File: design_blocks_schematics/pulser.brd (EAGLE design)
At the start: 160 x 100 mm, 52 parts

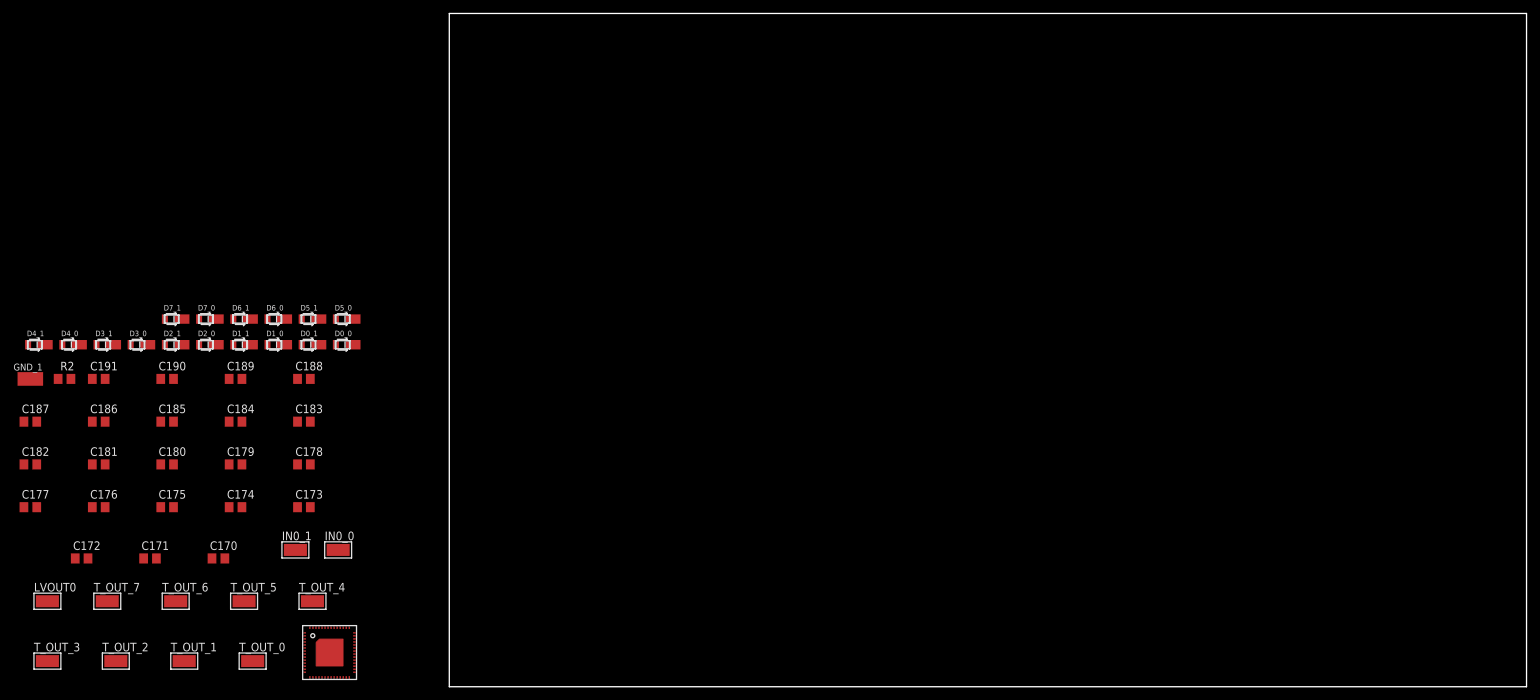
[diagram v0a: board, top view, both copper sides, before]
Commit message: added design block for sthv800 pulser chip
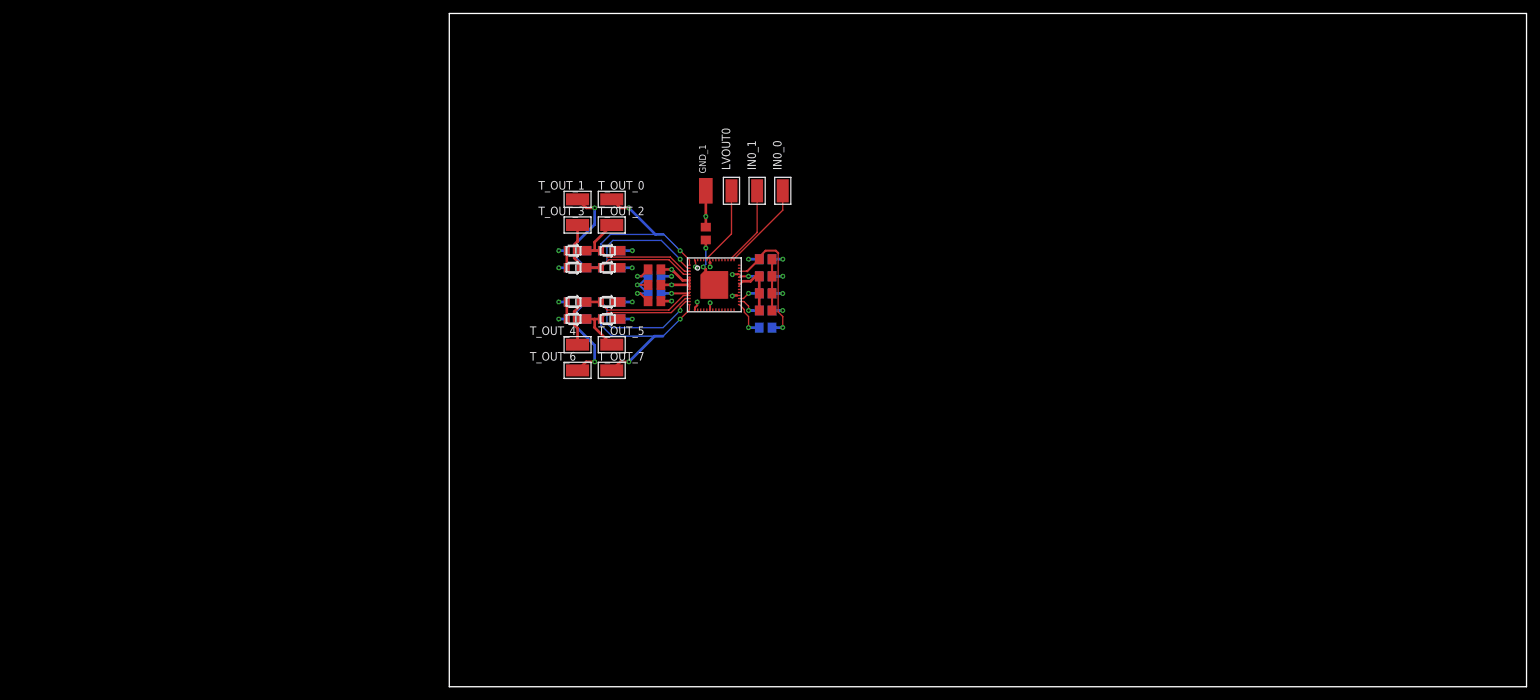
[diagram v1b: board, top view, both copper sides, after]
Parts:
- removed C171, C173, C176, C179, C186, C187, C188, C189: 220n 100V, rcl:C0805
- moved LVOUT0 118.5 mm to (41.9, 73.7), turned to 90 degrees
- moved C177 114.5 mm to (47.0, 61.0), flipped to the bottom
- moved C182 113.4 mm to (47.0, 63.5)
- moved C172 109.9 mm to (47.0, 61.0), turned to 180 degrees
- moved R2 104.4 mm to (47.0, 53.3), flipped to the bottom, turned to 180 degrees
- moved GND_1 104.1 mm to (38.1, 73.7), turned to 90 degrees
- moved C181 102.3 mm to (47.0, 58.4), flipped to the bottom, turned to 180 degrees
- moved T_OUT_3 102.0 mm to (19.1, 68.6)
- moved T_OUT_2 98.1 mm to (24.1, 68.6)
- moved C175 93.6 mm to (47.0, 55.9), turned to 180 degrees
- moved C180 91.8 mm to (47.0, 55.9), flipped to the bottom, turned to 180 degrees
- moved T_OUT_1 90.1 mm to (19.1, 72.4)
- moved C170 87.0 mm to (38.1, 67.3), turned to 90 degrees
- moved IN0_1 86.9 mm to (45.7, 73.7), turned to 90 degrees
- moved T_OUT_0 86.9 mm to (24.1, 72.4)
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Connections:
- removed net INX_1_0: IN0_1.1
- removed net PWM_INT0: IN0_0.1
- net GND: no longer C171.1, C173.1, C176.1, C179.1, C186.2, C187.2, C188.2, C189.1
- net HVM: no longer C186.1, C187.1, C188.1
- net HVM_CW: no longer C189.2
- net HVP: no longer C171.2, C173.2, C176.2
- net HVP_CW: no longer C179.2
- net IN0_0: now also IN0_0.1
- net IN0_1: now also IN0_1.1
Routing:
- net GND: track 0.00 -> 39.6 mm, vias 0 -> 14
- net OUT_1: track 0.00 -> 34.4 mm, vias 0 -> 2
- net OUT_6: track 0.00 -> 34.3 mm, vias 0 -> 2
- net OUT_0: track 0.00 -> 29.4 mm, vias 0 -> 2
- net OUT_7: track 0.00 -> 29.4 mm, vias 0 -> 2
- net OUT_4: track 0.00 -> 24.4 mm
- net OUT_3: track 0.00 -> 24.2 mm
- net HVM: track 0.00 -> 22.5 mm, vias 0 -> 7
- net OUT_5: track 0.00 -> 21.8 mm
- net OUT_2: track 0.00 -> 21.8 mm
- net DVDD: track 0.00 -> 20.6 mm, vias 0 -> 1
- net HVP: track 0.00 -> 17.0 mm, vias 0 -> 4
- net IN0_0: track 0.00 -> 13.3 mm
- net IN0_1: track 0.00 -> 11.9 mm
- net LVOUT_0: track 0.00 -> 11.8 mm
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
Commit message: pulser layout WIP
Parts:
- moved GND_1 11.4 mm to (47.3, 66.8), turned to 0 degrees
- moved LVOUT0 9.30 mm to (39.1, 82.5)
- moved C170 7.92 mm to (32.6, 73.0)
- moved IN0_0 4.60 mm to (47.2, 69.7), turned to 0 degrees
- moved IN0_1 1.89 mm to (47.2, 72.4), turned to 0 degrees
- moved C175 1.52 mm to (47.0, 57.4)
- moved C174 1.03 mm to (47.0, 59.5)
- moved C172 0.54 mm to (47.0, 61.5)
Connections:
- new net VDD: R2.2
- net DVDD: no longer R2.2
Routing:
- net IN3_0: track 0.00 -> 18.2 mm
- net IN3_1: track 0.00 -> 17.9 mm
- net IN2_1: track 0.00 -> 17.1 mm
- net LVOUT_5: track 0.00 -> 16.6 mm
- net DVDD: track 20.6 -> 4.37 mm, vias 1 -> 0
- net LVOUT_4: track 0.00 -> 16.2 mm
- net IN2_0: track 0.00 -> 16.0 mm
- net LVOUT_6: track 0.00 -> 15.8 mm
- net IN1_1: track 0.00 -> 15.5 mm
- net IN1_0: track 0.00 -> 14.8 mm
- net LVOUT_1: track 0.00 -> 13.8 mm
- net GND: track 39.6 -> 27.2 mm, vias 14 -> 8
- net LVOUT_2: track 0.00 -> 10.5 mm
- net LVOUT_7: track 0.00 -> 9.98 mm
- net IN4_0: track 0.00 -> 9.46 mm
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
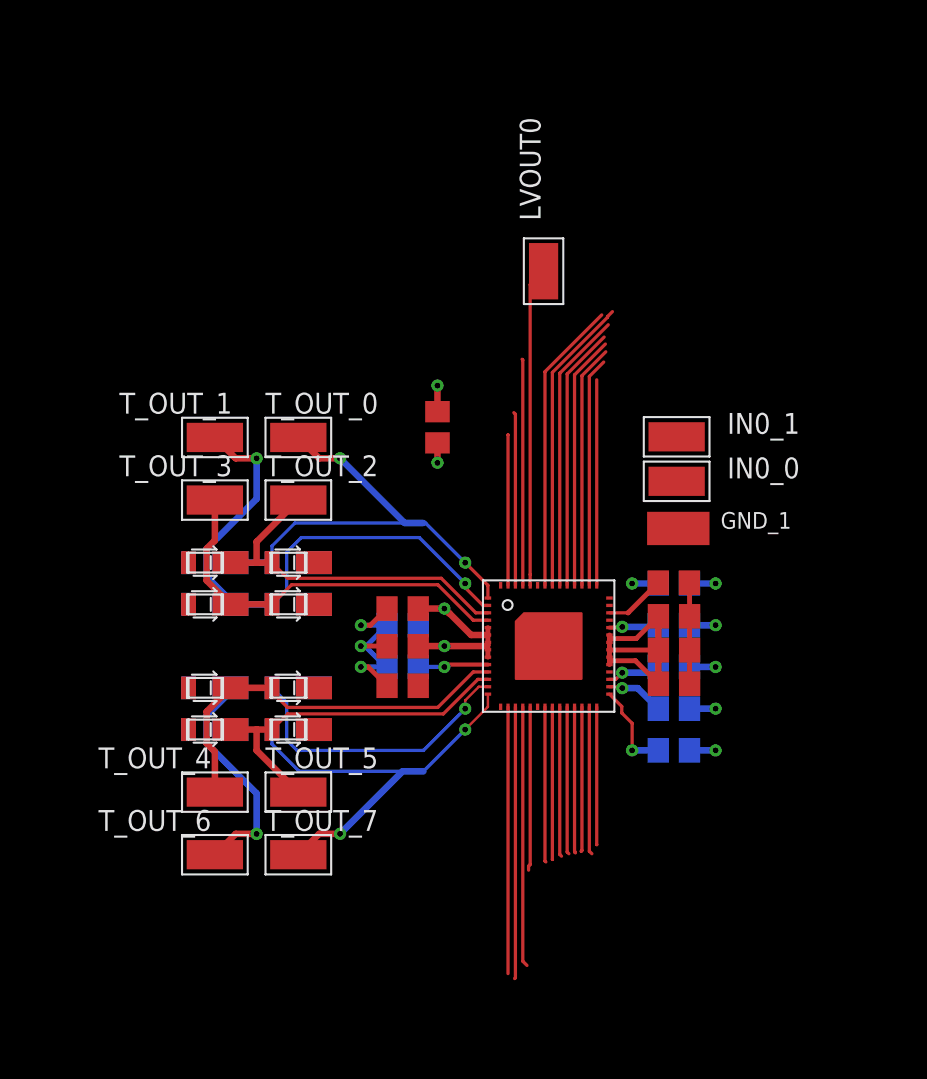
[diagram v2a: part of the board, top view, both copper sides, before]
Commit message: pulser layout done
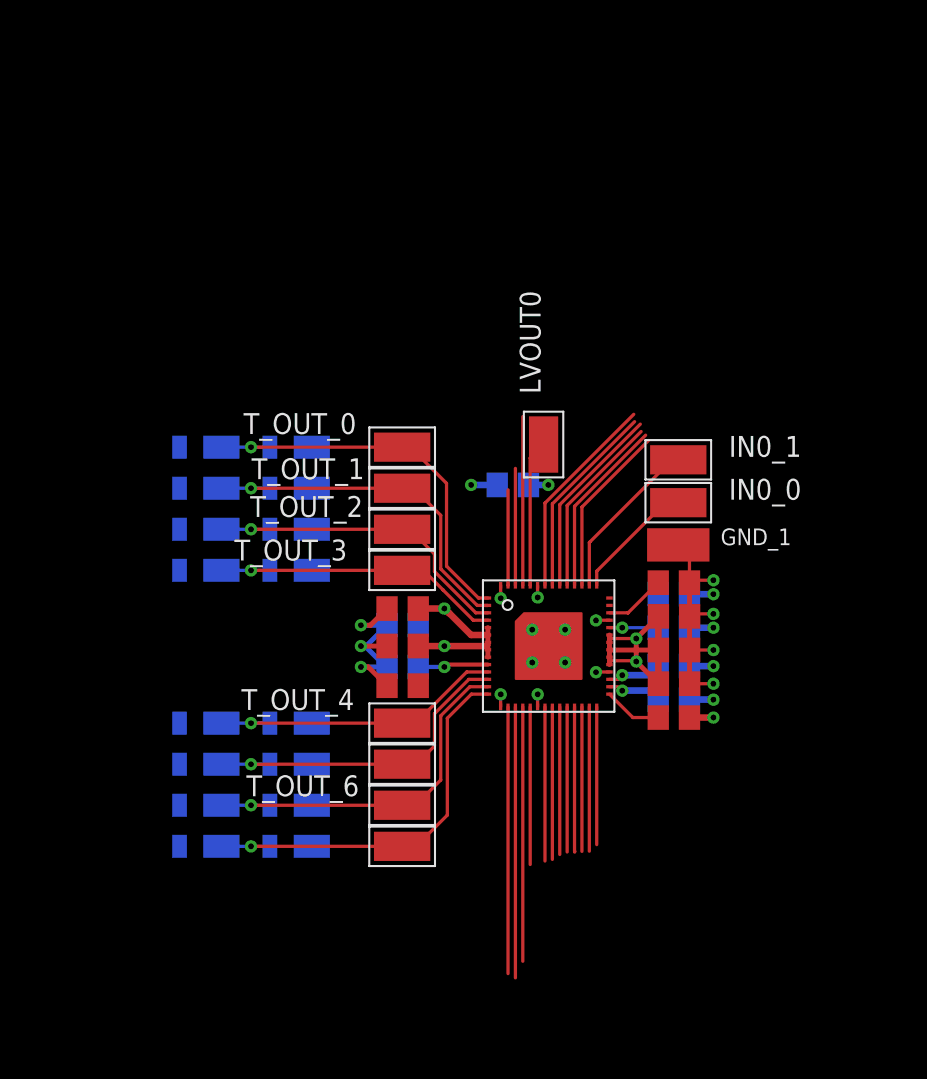
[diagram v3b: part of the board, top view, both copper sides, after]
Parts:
- moved T_OUT_3 12.2 mm to (30.4, 64.3)
- moved T_OUT_4 12.1 mm to (30.4, 55.0)
- moved T_OUT_1 11.8 mm to (30.4, 69.3)
- moved T_OUT_6 11.8 mm to (30.4, 50.0)
- moved LVOUT0 10.6 mm to (39.1, 72.0)
- moved D6_1 7.17 mm to (18.5, 50.0)
- moved D6_0 7.15 mm to (24.0, 50.0)
- moved D7_1 7.13 mm to (18.5, 47.5)
- moved D7_0 7.11 mm to (24.0, 47.5)
- moved D1_1 7.09 mm to (18.5, 69.3)
- moved D1_0 7.07 mm to (24.0, 69.3)
- moved D0_1 7.05 mm to (18.5, 71.8)
- moved D0_0 7.03 mm to (24.0, 71.8)
- moved T_OUT_2 6.57 mm to (30.4, 66.8)
- moved T_OUT_5 6.54 mm to (30.4, 52.5)
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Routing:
- net GND: track 27.2 -> 39.9 mm, vias 8 -> 18
- net OUT_1: track 34.4 -> 22.2 mm, vias 2 -> 1
- net OUT_6: track 34.3 -> 22.6 mm, vias 2 -> 1
- net LVOUT_0: track 19.5 -> 8.91 mm
- net IN3_0: track 18.2 -> 12.0 mm
- net OUT_4: track 24.4 -> 18.7 mm, vias 0 -> 1
- net OUT_3: track 24.2 -> 18.6 mm, vias 0 -> 1
- net OUT_0: track 29.4 -> 24.1 mm, vias 2 -> 1
- net IN3_1: track 17.9 -> 12.6 mm
- net IN2_1: track 17.1 -> 11.8 mm
- net IN0_0: track 12.5 -> 7.55 mm
- net IN2_0: track 16.0 -> 11.2 mm
- net OUT_7: track 29.4 -> 24.7 mm, vias 2 -> 1
- net IN1_1: track 15.5 -> 10.9 mm
- net IN1_0: track 14.8 -> 10.5 mm
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
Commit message: added backup files of eagle
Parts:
- moved C170 40.4 mm to (22.6, 31.8)
- moved C172 40.4 mm to (32.5, 23.8)
- moved C174 40.4 mm to (32.5, 21.8)
- moved C175 40.4 mm to (32.5, 19.7)
- moved C177 40.4 mm to (32.4, 23.1)
- moved C178 40.4 mm to (32.4, 25.1)
- moved C180 40.4 mm to (32.4, 18.7)
- moved C181 40.4 mm to (32.4, 20.8)
- moved C183 40.4 mm to (15.9, 24.3)
- moved C184 40.4 mm to (15.9, 22.0)
- moved C185 40.4 mm to (15.9, 19.6)
- moved C190 40.4 mm to (15.9, 20.7)
- moved C191 40.4 mm to (15.9, 23.3)
- moved D4_0 40.4 mm to (9.45, 17.3)
- moved D4_1 40.4 mm to (3.95, 17.3)
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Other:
- board size 160 x 100 mm -> 36.5 x 38 mm

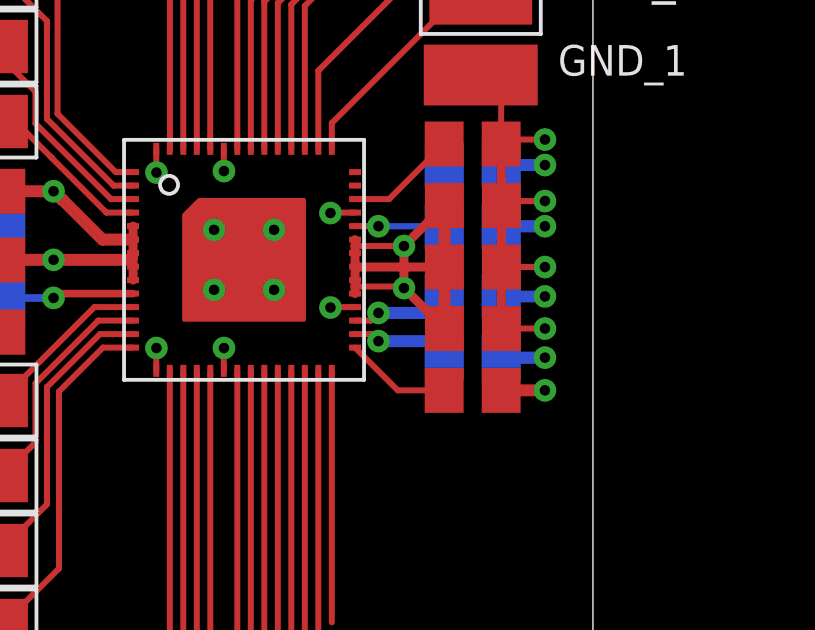
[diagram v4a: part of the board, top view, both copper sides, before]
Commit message: sthv800 update: connected dvdd & vddp
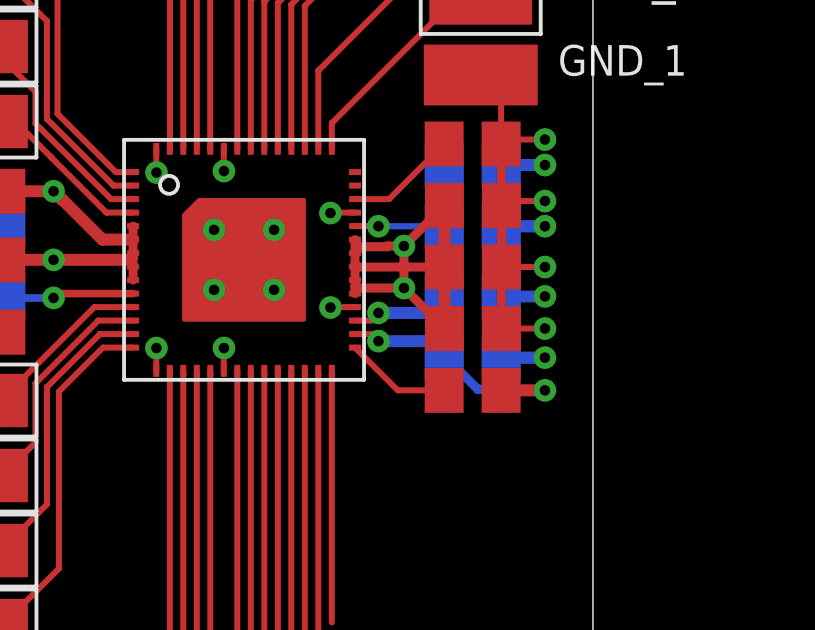
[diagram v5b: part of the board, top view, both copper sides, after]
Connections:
- removed net DVDD: C182.1, STHV_0.DVDD
- removed net VDD: R2.2
- net VDDP: now also C182.1, R2.2, STHV_0.DVDD
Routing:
- net VDDP: track 3.37 -> 15.4 mm, vias 1 -> 2
- net DVDD: track 4.37 -> 0.00 mm
- net VDD: track 1.46 -> 0.00 mm, vias 1 -> 0
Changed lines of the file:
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@@
 <contactref element="D5_0" pad="C"/>
 <contactref element="D6_0" pad="C"/>
-<wire x1="28.52" y1="22.665" x2="28.52" y2="22.45" width="0.3" layer="1"/>
-<wire x1="28.52" y1="22.45" x2="28.52" y2="21.75" width="0.3" layer="1"/>
+<wire x1="28.52" y1="22.665" x2="28.52" y2="21.75" width="0.3" layer="1"/>
 <wire x1="28.52" y1="21.75" x2="28.52" y2="21.1" width="0.3" layer="1"/>
-<wire x1="28.52" y1="21.1" x2="28.52" y2="20.865" width="0.3" layer="1"/>
 <wire x1="31.5" y1="23.8" x2="30.15" y2="22.45" width="0.3" layer="1"/>
-<wire x1="30.15" y1="22.45" x2="28.52" y2="22.45" width="0.2" layer="1"/>
 <wire x1="31.5" y1="21.75" x2="28.52" y2="21.75" width="0.3" layer="1"/>
 <wire x1="31.5" y1="19.7" x2="30.15" y2="21.05" width="0.3" layer="1"/>
-<wire x1="30.15" y1="21.05" x2="30.1" y2="21.1" width="0.3" layer="1"/>
-<wire x1="30.1" y1="21.1" x2="28.52" y2="21.1" width="0.2" layer="1"/>
 <via x="30.15" y="22.45" extent="1-16" drill="0.35"/>
 <via x="30.15" y="21.05" extent="1-16" drill="0.35"/>
 <wire x1="30.15" y1="22.45" x2="30.15" y2="21.05" width="0.3" layer="1"/>
-<wire x1="28.52" y1="21.765" x2="28.52" y2="22.215" width="0" layer="19" extent="1-1"/>
+<wire x1="29.5829125" y1="22.427" x2="29.6059125" y2="22.45" width="0.3048" layer="1"/>
+<wire x1="29.6059125" y1="22.45" x2="30.15" y2="22.45" width="0.3048" layer="1"/>
+<wire x1="28.52" y1="22.215" x2="28.732" y2="22.427" width="0.3048" layer="1"/>
+<wire x1="28.732" y1="22.427" x2="29.5829125" y2="22.427" width="0.3048" layer="1"/>
+<wire x1="28.52" y1="20.865" x2="28.52" y2="21.1" width="0.3048" layer="1"/>
+<wire x1="28.52" y1="21.1" x2="28.57" y2="21.05" width="0.3048" layer="1"/>
+<wire x1="28.57" y1="21.05" x2="30.15" y2="21.05" width="0.3048" layer="1"/>
 <wire x1="28.52" y1="21.315" x2="28.52" y2="21.765" width="0" layer="19" extent="1-1"/>
-<wire x1="28.52" y1="22.665" x2="28.52" y2="22.215" width="0" layer="19" extent="1-1"/>
+<wire x1="28.52" y1="22.215" x2="28.52" y2="21.765" width="0" layer="19" extent="1-1"/>
 <wire x1="10.4" y1="17.3" x2="28.52" y2="20.865" width="0" layer="19" extent="1-16"/>
 <wire x1="10.4" y1="14.8" x2="10.4" y2="17.3" width="0" layer="19" extent="16-16"/>
@@
 <wire x1="29.3" y1="19.415" x2="29.3" y2="19.28" width="0.2" layer="1"/>
 <wire x1="29.2" y1="19.515" x2="29.3" y2="19.415" width="0.2" layer="1"/>
+<contactref element="R2" pad="2"/>
+<via x="34.85" y="17.64" extent="1-16" drill="0.35"/>
+<wire x1="33.39" y1="17.64" x2="34.85" y2="17.64" width="0.4" layer="1"/>
+<contactref element="C182" pad="1"/>
+<contactref element="STHV_0" pad="DVDD"/>
+<wire x1="31.17" y1="25.85" x2="31.49" y2="25.85" width="0.2" layer="1"/>
+<wire x1="28.52" y1="24.015" x2="29.655" y2="24.015" width="0.2" layer="1"/>
+<wire x1="29.655" y1="24.015" x2="31.49" y2="25.85" width="0.2" layer="1"/>
+<wire x1="31.49" y1="25.85" x2="31.49" y2="26.17" width="0.3" layer="1"/>
+<wire x1="29.3" y1="19.28" x2="31.00895" y2="19.28" width="0.3048" layer="16"/>
+<wire x1="34.8148" y1="17.6752" x2="34.85" y2="17.64" width="0.3048" layer="16"/>
+<wire x1="31.00895" y1="19.28" x2="32.61375" y2="17.6752" width="0.3048" layer="16"/>
+<wire x1="32.61375" y1="17.6752" x2="34.8148" y2="17.6752" width="0.3048" layer="16"/>
+<wire x1="28.52" y1="19.515" x2="28.52" y2="24.015" width="0" layer="19" extent="1-1"/>
 </signal>
 <signal name="VDDM" class="1">
@@
 <contactref element="STHV_0" pad="LVOUT_8"/>
 <wire x1="23.695" y1="18.29" x2="23.695" y2="8.695" width="0.2" layer="1"/>
-</signal>
-<signal name="DVDD">
-<contactref element="C182" pad="1"/>
-<contactref element="STHV_0" pad="DVDD"/>
-<wire x1="31.17" y1="25.85" x2="31.49" y2="25.85" width="0.2" layer="1"/>
-<wire x1="28.52" y1="24.015" x2="29.655" y2="24.015" width="0.2" layer="1"/>
-<wire x1="29.655" y1="24.015" x2="31.49" y2="25.85" width="0.2" layer="1"/>
-<wire x1="31.49" y1="25.85" x2="31.49" y2="26.17" width="0.3" layer="1"/>
 </signal>
 <signal name="IN4_0">
@@
 <wire x1="2.35" y1="9.8" x2="2.35" y2="12.3" width="0" layer="19" extent="16-16"/>
 </signal>
-<signal name="VDD">
-<contactref element="R2" pad="2"/>
-<via x="34.85" y="17.64" extent="1-16" drill="0.35"/>
-<wire x1="33.39" y1="17.64" x2="34.85" y2="17.64" width="0.4" layer="1"/>
-</signal>
 <signal name="N$5">
